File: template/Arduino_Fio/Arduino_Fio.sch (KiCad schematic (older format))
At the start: 2 parts, among them P1 Digital, P2 Analog

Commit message: rebuilt shematic and fix librairie
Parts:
- removed P1: Digital, Socket_Arduino_Fio:Socket_Strip_Straight_1x14, symbol CONN_14
- removed P2: Analog, Socket_Arduino_Fio:Socket_Strip_Straight_1x14, symbol CONN_14
- added P1: Digital, Socket_Arduino_Fio:Socket_Strip_Straight_1x14, symbol CONN_01X14
- added P2: Analog, Socket_Arduino_Fio:Socket_Strip_Straight_1x14, symbol CONN_01X14
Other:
- note added: "1"
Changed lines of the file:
@@
 LIBS:memory
 LIBS:xilinx
-LIBS:special
 LIBS:microcontrollers
 LIBS:dsp
@@
 Comment4 ""
 $EndDescr
-$Comp
-L CONN_14 P1
-U 1 1 551FCE8A
-P 9700 1725
-F 0 "P1" V 9670 1725 60  0000 C CNN
-F 1 "Digital" V 9780 1725 60  0000 C CNN
-F 2 "Socket_Arduino_Fio:Socket_Strip_Straight_1x14" H 9700 1725 60  0001 C CNN
-F 3 "" H 9700 1725 60  0000 C CNN
-	1    9700 1725
-	1    0    0    -1
-$EndComp
-$Comp
-L CONN_14 P2
-U 1 1 551FCED2
-P 10125 1725
-F 0 "P2" V 10095 1725 60  0000 C CNN
-F 1 "Analog" V 10205 1725 60  0000 C CNN
-F 2 "Socket_Arduino_Fio:Socket_Strip_Straight_1x14" H 10125 1725 60  0001 C CNN
-F 3 "" H 10125 1725 60  0000 C CNN
-	1    10125 1725
-	-1   0    0    -1
-$EndComp
-Text Label 8650 1275 0    60   ~ 0
+Text Label 8850 1250 0    60   ~ 0
 2
-Text Label 8650 1375 0    60   ~ 0
+Text Label 8850 1350 0    60   ~ 0
 3(**)
-Text Label 8650 1475 0    60   ~ 0
+Text Label 8850 1450 0    60   ~ 0
 4
-Text Label 8650 1575 0    60   ~ 0
+Text Label 8850 1550 0    60   ~ 0
 5(**)
-Text Label 8650 1675 0    60   ~ 0
+Text Label 8850 1650 0    60   ~ 0
 6(**)
-Text Label 8650 1775 0    60   ~ 0
+Text Label 8850 1750 0    60   ~ 0
 7
-Text Label 8650 1875 0    60   ~ 0
+Text Label 8850 1850 0    60   ~ 0
 8
-Text Label 8650 1975 0    60   ~ 0
+Text Label 8850 1950 0    60   ~ 0
 9(**)
-Text Label 8650 2075 0    60   ~ 0
+Text Label 8850 2050 0    60   ~ 0
 10(**/SCK)
-Text Label 8650 2175 0    60   ~ 0
+Text Label 8850 2150 0    60   ~ 0
 11(**/MOSI)
-Text Label 8650 2275 0    60   ~ 0
+Text Label 8850 2250 0    60   ~ 0
 12(MISO)
-Text Label 8650 2375 0    60   ~ 0
+Text Label 8850 2350 0    60   ~ 0
 13(SS)
-Text Label 10700 2375 0    60   ~ 0
+Text Label 10700 2350 0    60   ~ 0
 A7
-Text Label 10700 2275 0    60   ~ 0
+Text Label 10700 2250 0    60   ~ 0
 A6
-Text Label 10700 2175 0    60   ~ 0
+Text Label 10700 2150 0    60   ~ 0
 A5(SCL)
-Text Label 10700 2075 0    60   ~ 0
+Text Label 10700 2050 0    60   ~ 0
 A4(SDA)
-Text Label 10700 1975 0    60   ~ 0
+Text Label 10700 1950 0    60   ~ 0
 A3
-Text Label 10700 1875 0    60   ~ 0
+Text Label 10700 1850 0    60   ~ 0
 A2
-Text Label 10700 1775 0    60   ~ 0
+Text Label 10700 1750 0    60   ~ 0
 A1
-Text Label 10700 1675 0    60   ~ 0
+Text Label 10700 1650 0    60   ~ 0
 A0
-Text Label 10700 1575 0    60   ~ 0
+Text Label 10700 1550 0    60   ~ 0
 DTR
-Text Label 10700 1475 0    60   ~ 0
+Text Label 10700 1450 0    60   ~ 0
 TxO
-Text Label 10700 1375 0    60   ~ 0
+Text Label 10700 1350 0    60   ~ 0
 RxI
-Text Label 10700 1175 0    60   ~ 0
+Text Label 10700 1150 0    60   ~ 0
 AREF
-$Comp
-L GND #PWR01
-U 1 1 551FD34C
-P 9275 2550
-F 0 "#PWR01" H 9275 2550 30  0001 C CNN
-F 1 "GND" H 9275 2480 30  0001 C CNN
-F 2 "" H 9275 2550 60  0000 C CNN
-F 3 "" H 9275 2550 60  0000 C CNN
-	1    9275 2550
-	1    0    0    -1
-$EndComp
-$Comp
-L GND #PWR02
-U 1 1 551FD39C
-P 10625 2550
-F 0 "#PWR02" H 10625 2550 30  0001 C CNN
-F 1 "GND" H 10625 2480 30  0001 C CNN
-F 2 "" H 10625 2550 60  0000 C CNN
-F 3 "" H 10625 2550 60  0000 C CNN
-	1    10625 2550
-	1    0    0    -1
-$EndComp
-$Comp
-L +3.3V #PWR03
-U 1 1 551FD4E9
-P 9275 900
-F 0 "#PWR03" H 9275 860 30  0001 C CNN
-F 1 "+3.3V" H 9275 1010 30  0000 C CNN
-F 2 "" H 9275 900 60  0000 C CNN
-F 3 "" H 9275 900 60  0000 C CNN
-	1    9275 900
-	1    0    0    -1
-$EndComp
-$Comp
-L +3.3V #PWR04
-U 1 1 551FD521
-P 10550 900
-F 0 "#PWR04" H 10550 860 30  0001 C CNN
-F 1 "+3.3V" H 10550 1010 30  0000 C CNN
-F 2 "" H 10550 900 60  0000 C CNN
-F 3 "" H 10550 900 60  0000 C CNN
-	1    10550 900
-	1    0    0    -1
-$EndComp
 Text Notes 8600 575  0    60   ~ 0
 Shield Arduino Fio
-Wire Wire Line
-	8650 1275 9350 1275
-Wire Wire Line
-	8650 1375 9350 1375
-Wire Wire Line
-	8650 1475 9350 1475
-Wire Wire Line
-	8650 1575 9350 1575
-Wire Wire Line
-	8650 1675 9350 1675
-Wire Wire Line
-	8650 1775 9350 1775
-Wire Wire Line
-	8650 1875 9350 1875
-Wire Wire Line
-	8650 1975 9350 1975
-Wire Wire Line
-	8650 2075 9350 2075
-Wire Wire Line
-	8650 2175 9350 2175
-Wire Wire Line
-	8650 2275 9350 2275
-Wire Wire Line
-	8650 2375 9350 2375
-Wire Wire Line
-	10475 1175 11075 1175
-Wire Wire Line
-	10475 1375 11075 1375
-Wire Wire Line
-	10475 1475 11075 1475
-Wire Wire Line
-	10475 1575 11075 1575
-Wire Wire Line
-	10475 1675 11075 1675
-Wire Wire Line
-	10475 1775 11075 1775
-Wire Wire Line
-	10475 1875 11075 1875
-Wire Wire Line
-	10475 1975 11075 1975
-Wire Wire Line
-	10475 2075 11075 2075
-Wire Wire Line
-	10475 2175 11075 2175
-Wire Wire Line
-	10475 2275 11075 2275
-Wire Wire Line
-	10475 2375 11075 2375
-Wire Wire Line
-	10550 900  10550 1275
-Wire Wire Line
-	9275 1175 9275 2550
-Wire Wire Line
-	9350 1175 9275 1175
-Wire Wire Line
-	9275 900  9275 1075
-Wire Wire Line
-	9275 1075 9350 1075
-Wire Wire Line
-	10550 1275 10475 1275
-Wire Wire Line
-	10625 1075 10625 2550
-Wire Wire Line
-	10625 1075 10475 1075
 Wire Notes Line
 	8575 475  8575 2675
@@
 Wire Notes Line
 	8575 2675 11225 2675
+$Comp
+L CONN_01X14 P1
+U 1 1 56D705A1
+P 9750 1700
+F 0 "P1" H 9750 2450 50  0000 C CNN
+F 1 "Digital" V 9850 1700 50  0000 C CNN
+F 2 "Socket_Arduino_Fio:Socket_Strip_Straight_1x14" H 9750 1700 50  0001 C CNN
+F 3 "" H 9750 1700 50  0000 C CNN
+	1    9750 1700
+	1    0    0    -1
+$EndComp
+$Comp
+L CONN_01X14 P2
+U 1 1 56D706EC
+P 10100 1700
+F 0 "P2" H 10100 2450 50  0000 C CNN
+F 1 "Analog" V 10200 1700 50  0000 C CNN
+F 2 "Socket_Arduino_Fio:Socket_Strip_Straight_1x14" H 10100 1700 50  0001 C CNN
+F 3 "" H 10100 1700 50  0000 C CNN
+	1    10100 1700
+	-1   0    0    -1
+$EndComp
+$Comp
+L +3.3V #PWR01
+U 1 1 56D707AD
+P 9450 950
+F 0 "#PWR01" H 9450 800 50  0001 C CNN
+F 1 "+3.3V" H 9450 1090 50  0000 C CNN
+F 2 "" H 9450 950 50  0000 C CNN
+F 3 "" H 9450 950 50  0000 C CNN
+	1    9450 950
+	1    0    0    -1
+$EndComp
+Wire Wire Line
+	9550 1050 9450 1050
+Wire Wire Line
+	9450 1050 9450 950
+Wire Wire Line
+	9550 1150 9450 1150
+$Comp
+L GND #PWR02
+U 1 1 56D7084A
+P 9450 2450
+F 0 "#PWR02" H 9450 2200 50  0001 C CNN
+F 1 "GND" H 9450 2300 50  0000 C CNN
+F 2 "" H 9450 2450 50  0000 C CNN
+F 3 "" H 9450 2450 50  0000 C CNN
+	1    9450 2450
+	1    0    0    -1
+$EndComp
+Wire Wire Line
+	9450 1150 9450 2450
+Wire Wire Line
+	8850 1250 9550 1250
+Wire Wire Line
+	8850 1350 9550 1350
+Wire Wire Line
+	8850 1450 9550 1450
+Wire Wire Line
+	9550 1550 8850 1550
+Wire Wire Line
+	8850 1650 9550 1650
+Wire Wire Line
+	8850 1750 9550 1750
+Wire Wire Line
+	8850 1850 9550 1850
+Wire Wire Line
+	9550 1950 8850 1950
+Wire Wire Line
+	8850 2050 9550 2050
+Wire Wire Line
+	8850 2150 9550 2150
+Wire Wire Line
+	8850 2250 9550 2250
+Wire Wire Line
+	9550 2350 8850 2350
+Wire Wire Line
+	10300 1250 10400 1250
+Wire Wire Line
+	10400 1250 10400 950
+$Comp
+L +3.3V #PWR03
+U 1 1 56D70A18
+P 10400 950
+F 0 "#PWR03" H 10400 800 50  0001 C CNN
+F 1 "+3.3V" H 10400 1090 50  0000 C CNN
+F 2 "" H 10400 950 50  0000 C CNN
+F 3 "" H 10400 950 50  0000 C CNN
+	1    10400 950
+	1    0    0    -1
+$EndComp
+Wire Wire Line
+	10300 1050 10500 1050
+Wire Wire Line
+	10500 1050 10500 2450
+$Comp
+L GND #PWR04
+U 1 1 56D70A5E
+P 10500 2450
+F 0 "#PWR04" H 10500 2200 50  0001 C CNN
+F 1 "GND" H 10500 2300 50  0000 C CNN
+F 2 "" H 10500 2450 50  0000 C CNN
+F 3 "" H 10500 2450 50  0000 C CNN
+	1    10500 2450
+	1    0    0    -1
+$EndComp
+Wire Wire Line
+	10300 1150 10700 1150
+Wire Wire Line
+	10700 1350 10300 1350
+Wire Wire Line
+	10700 1450 10300 1450
+Wire Wire Line
+	10700 1550 10300 1550
+Wire Wire Line
+	10700 1650 10300 1650
+Wire Wire Line
+	10300 1750 10700 1750
+Wire Wire Line
+	10700 1850 10300 1850
+Wire Wire Line
+	10700 1950 10300 1950
+Wire Wire Line
+	10700 2050 10300 2050
+Wire Wire Line
+	10300 2150 10700 2150
+Wire Wire Line
+	10700 2250 10300 2250
+Wire Wire Line
+	10700 2350 10300 2350
+Text Notes 9850 1050 0    60   ~ 0
+1
 $EndSCHEMATC

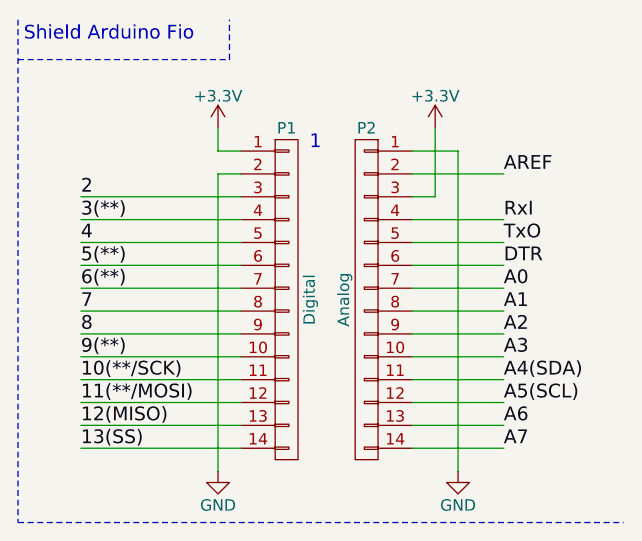
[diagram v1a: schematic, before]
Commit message: fix template
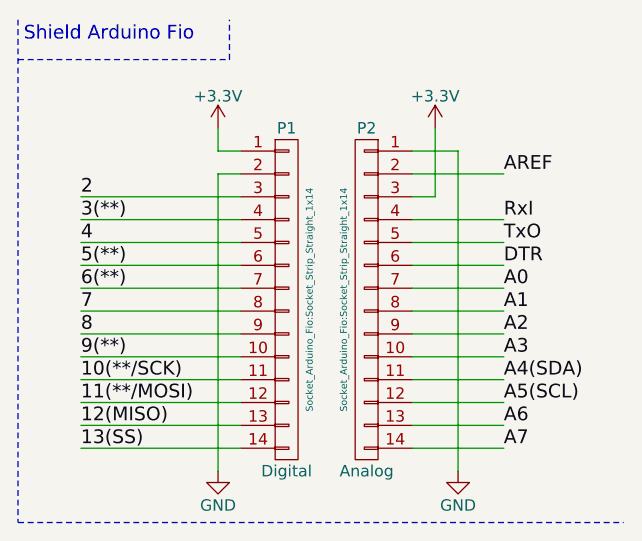
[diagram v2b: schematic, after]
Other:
- note removed: "1"
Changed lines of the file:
@@
 P 9750 1700
 F 0 "P1" H 9750 2450 50  0000 C CNN
-F 1 "Digital" V 9850 1700 50  0000 C CNN
-F 2 "Socket_Arduino_Fio:Socket_Strip_Straight_1x14" H 9750 1700 50  0001 C CNN
+F 1 "Digital" H 9750 950 50  0000 C CNN
+F 2 "Socket_Arduino_Fio:Socket_Strip_Straight_1x14" V 9850 1700 30  0000 C CNN
 F 3 "" H 9750 1700 50  0000 C CNN
 	1    9750 1700
@@
 P 10100 1700
 F 0 "P2" H 10100 2450 50  0000 C CNN
-F 1 "Analog" V 10200 1700 50  0000 C CNN
-F 2 "Socket_Arduino_Fio:Socket_Strip_Straight_1x14" H 10100 1700 50  0001 C CNN
+F 1 "Analog" H 10100 950 50  0000 C CNN
+F 2 "Socket_Arduino_Fio:Socket_Strip_Straight_1x14" V 10200 1700 30  0000 C CNN
 F 3 "" H 10100 1700 50  0000 C CNN
 	1    10100 1700
@@
 Wire Wire Line
 	10700 2350 10300 2350
-Text Notes 9850 1050 0    60   ~ 0
-1
 $EndSCHEMATC

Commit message: Template Arduino : Fix pin order SS, MOSI, MISO, SCK
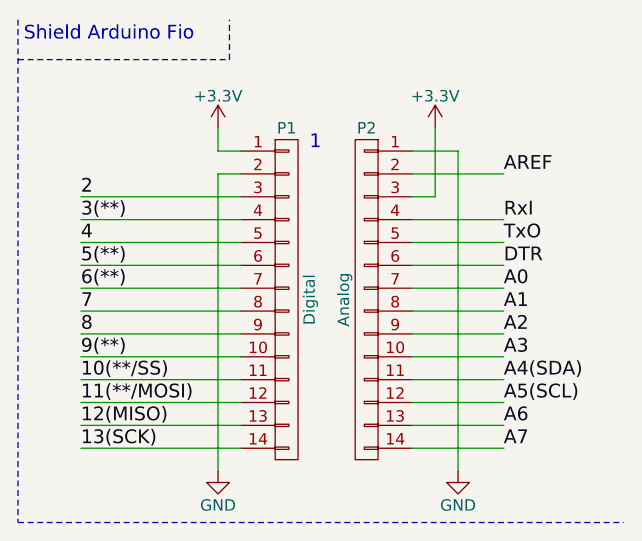
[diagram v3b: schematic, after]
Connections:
- net 10(**/SCK) renamed 10(**/SS)
- net 13(SS) renamed 13(SCK)
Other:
- note added: "1"
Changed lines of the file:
@@
 9(**)
 Text Label 8850 2050 0    60   ~ 0
-10(**/SCK)
+10(**/SS)
 Text Label 8850 2150 0    60   ~ 0
 11(**/MOSI)
@@
 12(MISO)
 Text Label 8850 2350 0    60   ~ 0
-13(SS)
+13(SCK)
 Text Label 10700 2350 0    60   ~ 0
 A7
@@
 P 9750 1700
 F 0 "P1" H 9750 2450 50  0000 C CNN
-F 1 "Digital" H 9750 950 50  0000 C CNN
-F 2 "Socket_Arduino_Fio:Socket_Strip_Straight_1x14" V 9850 1700 30  0000 C CNN
+F 1 "Digital" V 9850 1700 50  0000 C CNN
+F 2 "Socket_Arduino_Fio:Socket_Strip_Straight_1x14" H 9750 1700 50  0001 C CNN
 F 3 "" H 9750 1700 50  0000 C CNN
 	1    9750 1700
@@
 P 10100 1700
 F 0 "P2" H 10100 2450 50  0000 C CNN
-F 1 "Analog" H 10100 950 50  0000 C CNN
-F 2 "Socket_Arduino_Fio:Socket_Strip_Straight_1x14" V 10200 1700 30  0000 C CNN
+F 1 "Analog" V 10200 1700 50  0000 C CNN
+F 2 "Socket_Arduino_Fio:Socket_Strip_Straight_1x14" H 10100 1700 50  0001 C CNN
 F 3 "" H 10100 1700 50  0000 C CNN
 	1    10100 1700
@@
 Wire Wire Line
 	10700 2350 10300 2350
+Text Notes 9850 1050 0    60   ~ 0
+1
 $EndSCHEMATC
